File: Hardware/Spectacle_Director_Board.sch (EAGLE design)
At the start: 68 parts, among them J2 I2C-TRRS, J3 Serial-TRRS, Q1 310mA/60V/1.6Ω, Q2 310mA/60V/1.6Ω, U1 AP2151, U2 ATSAMD21G-A, U3 3.3V, U4 W25Q32FV

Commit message: Minor adjustments post-engineer checklist.
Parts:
- removed C15: 47pF, SparkFun-Capacitors:47PF-0603-50V-5%
- removed R16: 330, SparkFun-Resistors:330OHM-0603-1/10W-1%
- removed R17: 10k, SparkFun-Resistors:10KOHM-0603-1/10W-1%
- added C12: 0.1uF, SparkFun-Capacitors:0.1UF-0603-25V-(+80/-20%)
- added R7: 10k, SparkFun-Resistors:10KOHM-0603-1/10W-1%
- added R8: 330, SparkFun-Resistors:330OHM-0603-1/10W-1%
- C11: value 0.1uF -> 47pF; device SparkFun-Capacitors:0.1UF-0603-25V-(+80/-20%) -> SparkFun-Capacitors:47PF-0603-50V-5%
- C13: value 0.1uF -> 0.22uF; device SparkFun-Capacitors:0.1UF-0603-25V-(+80/-20%) -> SparkFun-Capacitors:0.22UF-0603-25V-10%
- C14: value 0.22uF -> 0.1uF; device SparkFun-Capacitors:0.22UF-0603-25V-10% -> SparkFun-Capacitors:0.1UF-0603-25V-(+80/-20%)
- D10: value 0.5A/40V/420mV -> GREEN; device SparkFun-DiscreteSemi:DIODE-SCHOTTKY-PMEG4005EJ -> SparkFun-LED:LED-GREEN0603
- D4: value GREEN -> 0.5A/40V/420mV; device SparkFun-LED:LED-GREEN0603 -> SparkFun-DiscreteSemi:DIODE-SCHOTTKY-PMEG4005EJ
- D5: value PESD1CAN -> 0.5A/40V/420mV; device SparkFun-DiscreteSemi:PESD1CAN -> SparkFun-DiscreteSemi:DIODE-SCHOTTKY-PMEG4005EJ
- D6: value Yellow -> GREEN; device SparkFun-LED:LED-YELLOW0603 -> SparkFun-LED:LED-GREEN0603
- D7: value BLUE -> PESD1CAN; device SparkFun-LED:LED-BLUE0603 -> SparkFun-DiscreteSemi:PESD1CAN
- D8: value GREEN -> Yellow; device SparkFun-LED:LED-GREEN0603 -> SparkFun-LED:LED-YELLOW0603
- D9: value 0.5A/40V/420mV -> BLUE; device SparkFun-DiscreteSemi:DIODE-SCHOTTKY-PMEG4005EJ -> SparkFun-LED:LED-BLUE0603
- R10, R13: value 330 -> 10k; device SparkFun-Resistors:330OHM-0603-1/10W-1% -> SparkFun-Resistors:10KOHM-0603-1/10W-1%
- R11, R14: value 10k -> 100k; device SparkFun-Resistors:10KOHM-0603-1/10W-1% -> SparkFun-Resistors:100KOHM-0603-1/10W-1%
- R12, R15: value 100k -> 330; device SparkFun-Resistors:100KOHM-0603-1/10W-1% -> SparkFun-Resistors:330OHM-0603-1/10W-1%
- R5: value 1k -> 10k; device SparkFun-Resistors:1KOHM-0603-1/10W-1% -> SparkFun-Resistors:10KOHM-0603-1/10W-1%
- R6: value 10k -> 1k; device SparkFun-Resistors:10KOHM-0603-1/10W-1% -> SparkFun-Resistors:1KOHM-0603-1/10W-1%
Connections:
- net !RESET: now also R10.1; no longer R11.1
- net 3.3V: now also C12.1, C14.1, D4.C, R12.2, R15.2, R5.2, R6.1, R8.2; no longer C11.1, C13.1, D9.C, R11.2, R14.2, R16.2, R17.2, R5.1
- net A1_FSK-RX: now also C11.2, C13.1, D4.A, D5.C, R5.1, R7.2; no longer C14.1, C15.2, D10.C, D9.A, R17.1, R6.2
- net D13_LED1: now also R11.2; no longer R12.2
- net D6_BTN: now also R13.1; no longer R14.1
- net D7_LED2: now also R14.2; no longer R15.2
- net GND: now also C11.1, C12.2, C14.2, D5.A, D7.3, R11.1, R14.1, R7.1; no longer C11.2, C13.2, C15.1, D10.A, D5.3, R12.1, R15.1, R6.1
- net N$1: now also D10.A, R15.1; no longer D8.A, R16.1
- net N$10: now also D9.C; no longer D7.C
- net N$11: now also D6.A, R8.1; no longer D4.A, R9.1
- net N$12: now also D8.A, R9.1; no longer D6.A, R10.1
- net N$2: now also R6.2; no longer R5.2
- net N$7: now also D10.C; no longer D8.C
- net N$9: now also D9.A, R12.1; no longer D7.A, R13.1
- net RING1-RIGHT: now also D7.2; no longer D5.2
- net RX_LED: now also D8.C; no longer D6.C
- net TIP-LEFT: now also C13.2, D7.1; no longer C14.2, D5.1
- net TX_LED: now also D6.C; no longer D4.C
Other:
- moved on the sheet: C11, C13, C14, C8, C9, D1, D3, D6, D8, F1, J1, R10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

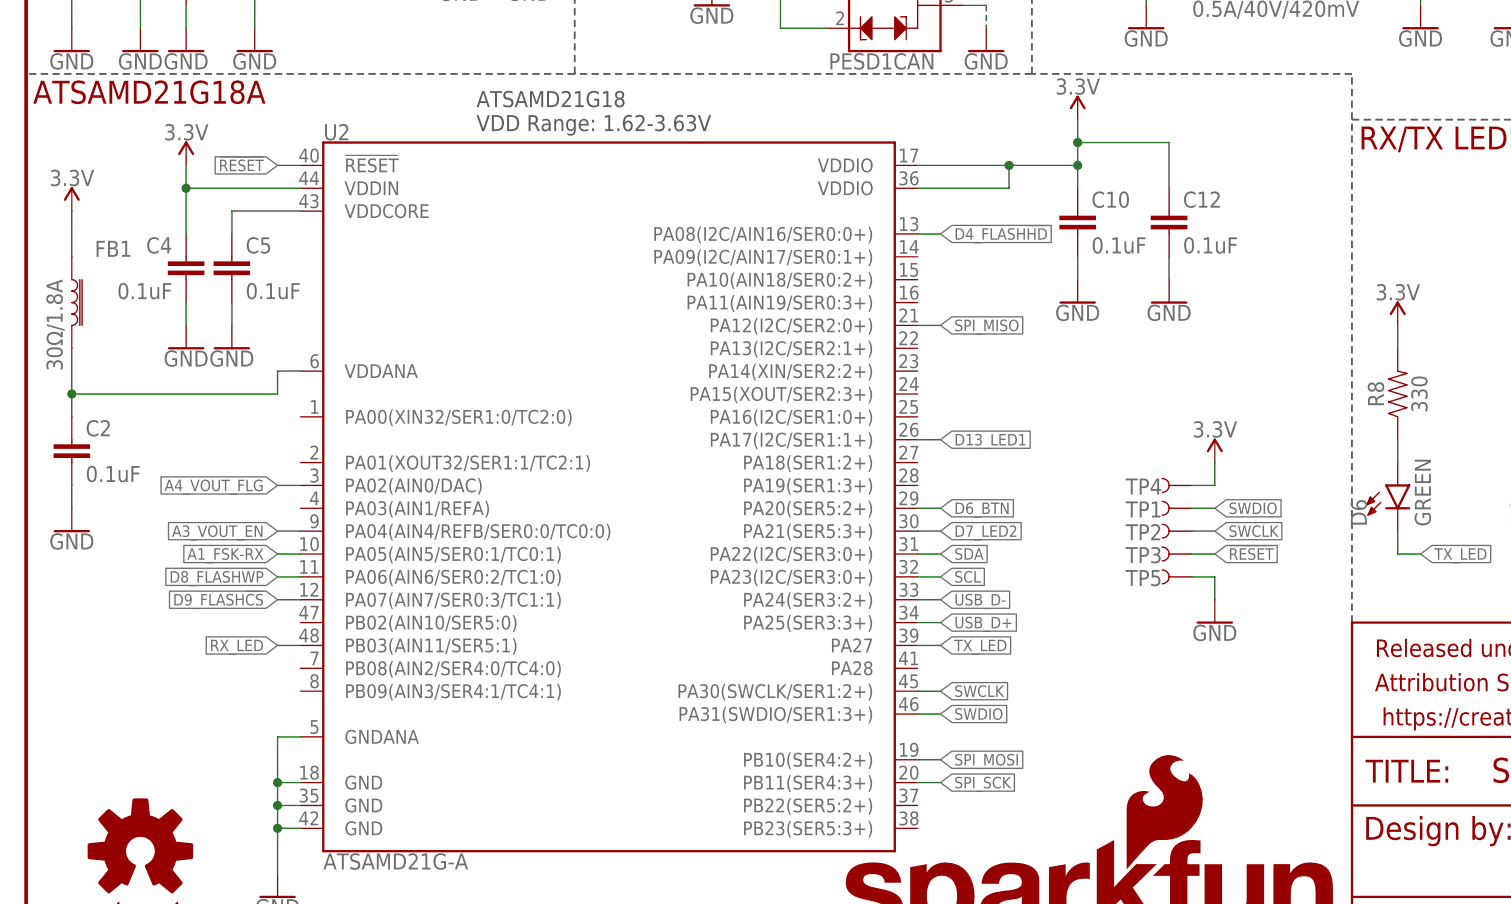
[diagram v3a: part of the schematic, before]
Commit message: Adding UART test points, 32.768kHz RTC crystal
- Moved flash down about 0.1" to accomodate uart test points
- Moved SWD test points to accomodate RTC crystal
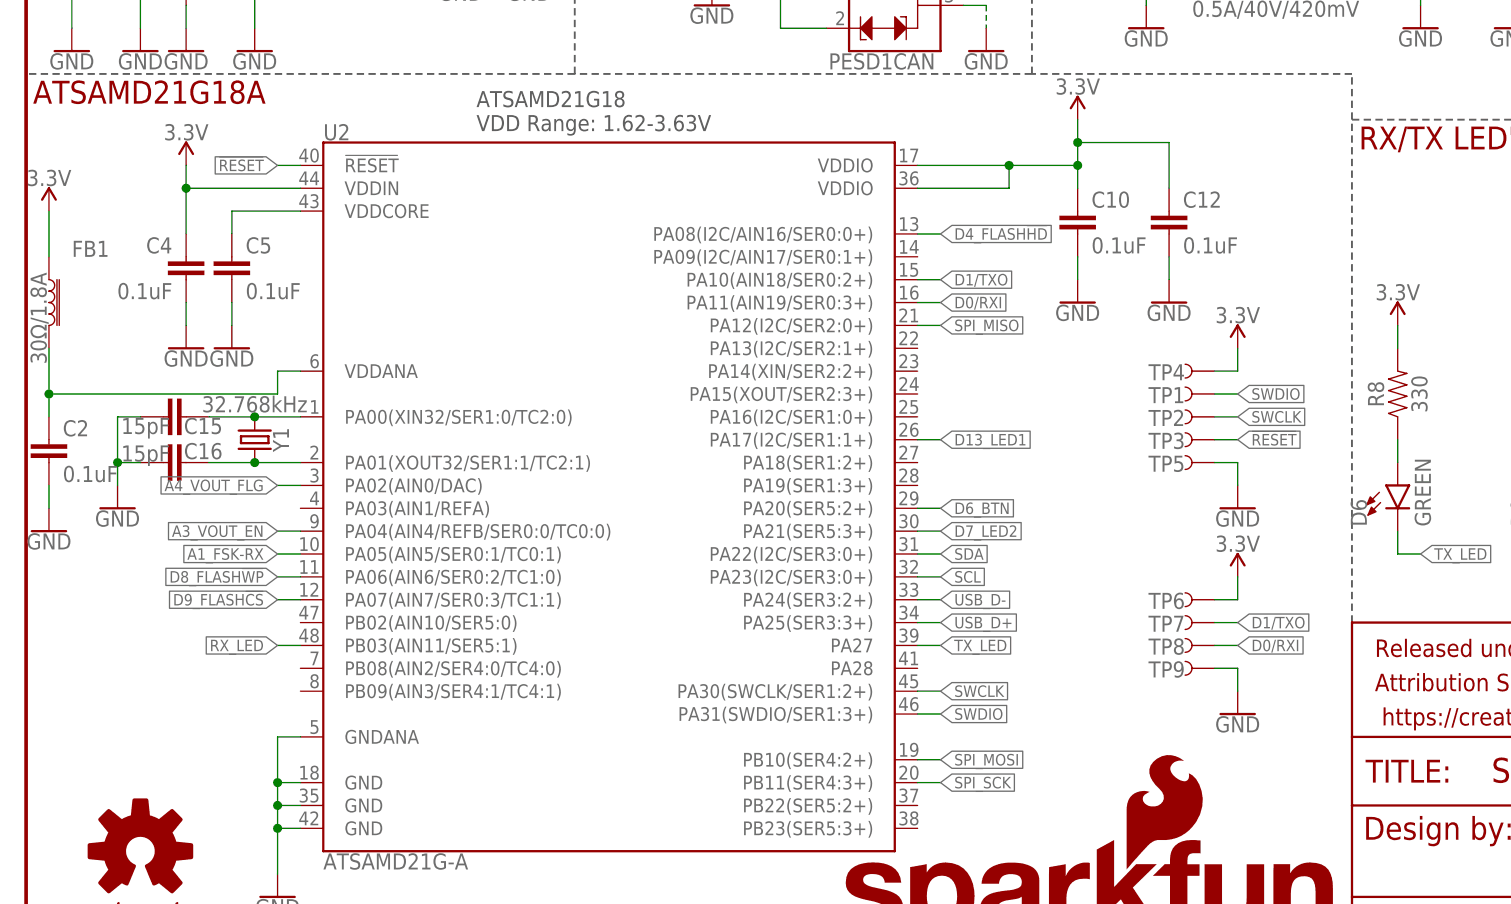
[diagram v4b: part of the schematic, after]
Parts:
- added C15, C16: 15pF, SparkFun-Capacitors:15PF-0603-50V-5%
- added TP6, TP7, TP8, TP9: TP-GND, SparkFun-Connectors:TEST-POINT3X5
- added Y1: 32.768kHz, SparkFun-Clocks:CRYSTAL-32.768KHZSMD-3.2X1.5
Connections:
- new net D0/RXI: TP8.1, U2.PA11(AIN19/SER0:3+)
- new net D1/TXO: TP7.1, U2.PA10(AIN18/SER0:2+)
- new net N$3: C15.2, U2.PA00(XIN32/SER1:0/TC2:0), Y1.2
- new net N$6: C16.2, U2.PA01(XOUT32/SER1:1/TC2:1), Y1.1
- net 3.3V: now also TP6.1
- net GND: now also C15.1, C16.1, TP9.1
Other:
- moved on the sheet: C2, FB1, TP1, TP2, TP3, TP4, TP5

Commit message: Spacing test points by 2mm, increasing via drill size.
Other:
- note added: "v05"
- note removed: "v04"
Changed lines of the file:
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@@
 <text x="99.06" y="154.94" size="1.524" layer="97">600mA out
 6V max in</text>
-<text x="238.76" y="10.16" size="2.54" layer="94" align="top-left">v04</text>
+<text x="238.76" y="10.16" size="2.54" layer="94" align="top-left">v05</text>
 <text x="172.72" y="13.716" size="2.54" layer="94" align="top-left">Mike Hord
 Jim Lindblom</text>

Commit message: Incrementing hardware to v10. No other changes.
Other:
- note added: "v10"
- note removed: "v05"
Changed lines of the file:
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@@
 <text x="99.06" y="154.94" size="1.524" layer="97">600mA out
 6V max in</text>
-<text x="238.76" y="10.16" size="2.54" layer="94" align="top-left">v05</text>
+<text x="238.76" y="10.16" size="2.54" layer="94" align="top-left">v10</text>
 <text x="172.72" y="13.716" size="2.54" layer="94" align="top-left">Mike Hord
 Jim Lindblom</text>
